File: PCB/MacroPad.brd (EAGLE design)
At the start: 76.2 x 76.2 mm, 42 parts, among them SW00 SWITCH-SMD-EVQP-P2602W, SW01 KEYSWITCH-PLAIN-MX-1U, SW02 KEYSWITCH-PLAIN-MX-1U, SW03 KEYSWITCH-PLAIN-MX-1U, SW04 KEYSWITCH-PLAIN-MX-1U, SW05 KEYSWITCH-PLAIN-MX-1U, SW06 KEYSWITCH-PLAIN-MX-1U, SW07 KEYSWITCH-PLAIN-MX-1U, SW08 KEYSWITCH-PLAIN-MX-1U, SW09 KEYSWITCH-PLAIN-MX-1U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

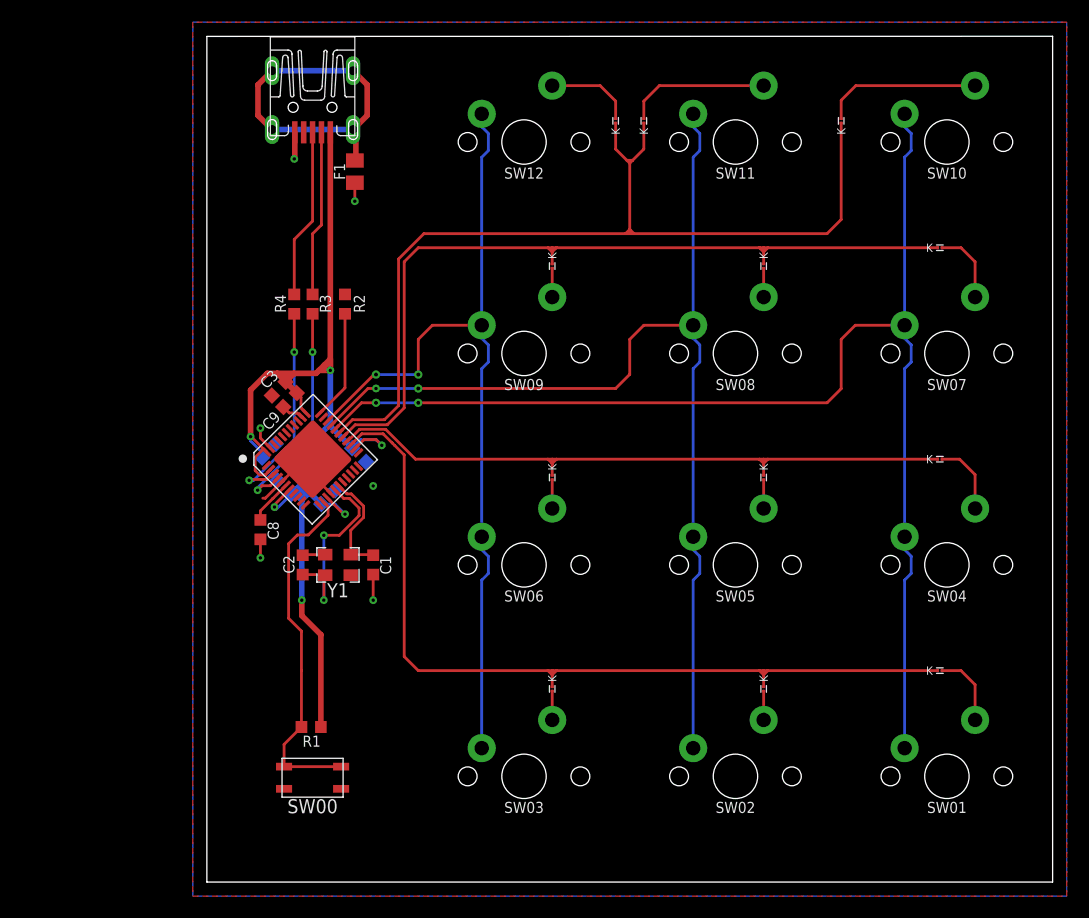
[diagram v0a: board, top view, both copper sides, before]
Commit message: Replace surface mount diodes with through hole
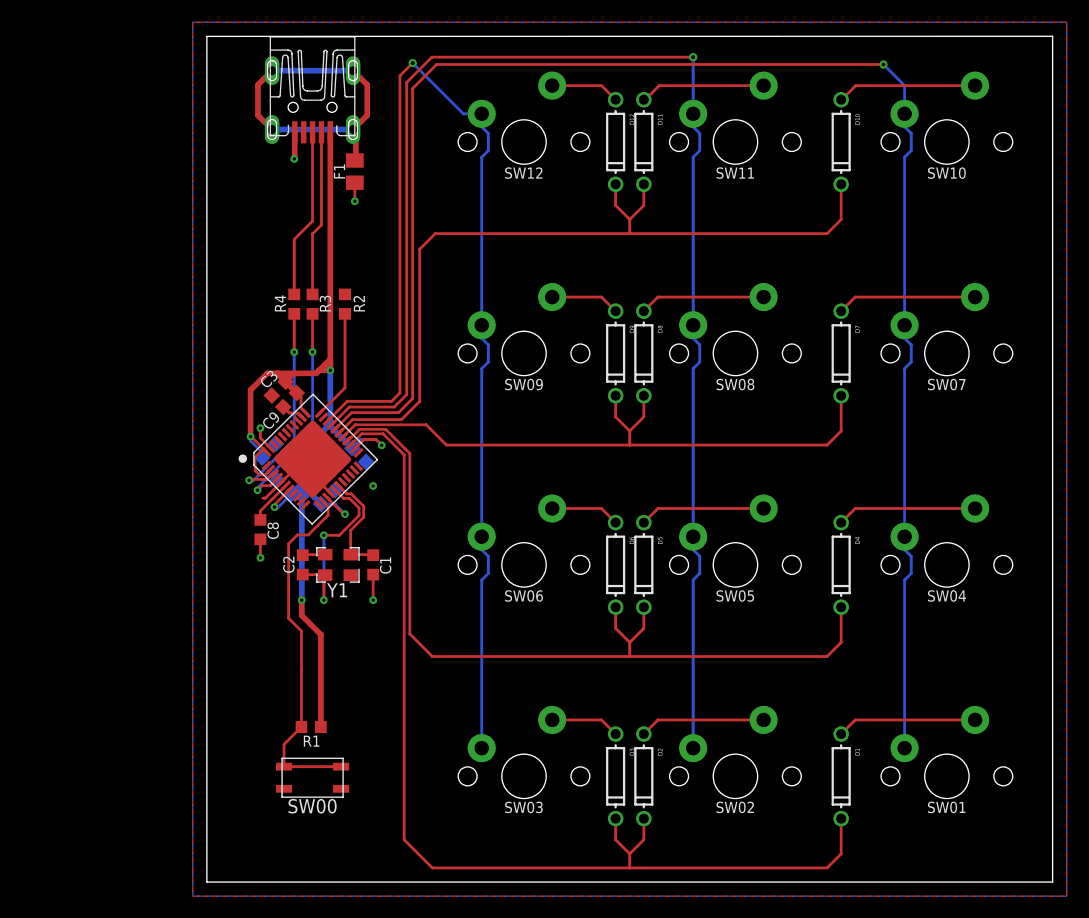
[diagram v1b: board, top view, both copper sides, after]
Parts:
- D1, D10, D11, D12, D2, D3, D4, D5, D6, D7, D8, D9: device Components:DFN0603-2 -> adafruit:DO-1N4148
- moved D8 13.4 mm to (39.4, 47.6)
- moved D2 13.4 mm to (39.4, 9.53)
- moved D5 13.4 mm to (39.4, 28.6)
- moved D1 13.0 mm to (57.1, 9.53), turned to 270 degrees
- moved D4 13.0 mm to (57.1, 28.6), turned to 270 degrees
- moved D7 13.0 mm to (57.1, 47.6), turned to 270 degrees
- moved D3 9.73 mm to (36.8, 9.53)
- moved D9 9.73 mm to (36.8, 47.6)
- moved D6 9.73 mm to (36.8, 28.6)
- moved D10 1.91 mm to (57.1, 66.7), turned to 270 degrees
- moved D11 1.91 mm to (39.4, 66.7), turned to 270 degrees
- moved D12 1.91 mm to (36.8, 66.7), turned to 270 degrees
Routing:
- net N$40: track 96.8 -> 126.6 mm, vias 2 -> 1
- net N$10: track 116.4 -> 143.2 mm, vias 2 -> 1
- net N$16: track 78.0 -> 104.5 mm, vias 2 -> 1
- net N$14: track 77.9 -> 93.5 mm
- net N$26: track 59.9 -> 75.3 mm
- net N$32: track 73.4 -> 58.5 mm
- net N$38: track 85.9 -> 73.1 mm
- net N$21: track 2.60 -> 11.3 mm
- net N$12: track 2.60 -> 11.3 mm
- net N$30: track 2.60 -> 11.3 mm
- net N$18: track 6.61 -> 12.6 mm
- net N$9: track 6.69 -> 12.6 mm
- net N$27: track 6.69 -> 12.6 mm
- net N$24: track 2.60 -> 6.24 mm
- net N$15: track 2.60 -> 6.24 mm
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
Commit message: Swap GFN for TQFP Chip -- board not updated
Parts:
- removed U$1: ATMEGA32U4-QFN44, Controller:QFN-44
- added U1: ATMEGA32U4-AUR, ATMEGA32U4-AUR:QFP80P1200X1200X120-44N
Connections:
- net GND: now also U1.15, U1.23, U1.35, U1.43, U1.5; no longer U$1.15, U$1.23, U$1.35, U$1.43, U$1.5, U$1.TAB
- net N$1: now also U1.16; no longer U$1.16
- net N$10: now also U1.29; no longer U$1.29
- net N$14: now also U1.25; no longer U$1.25
- net N$16: now also U1.31; no longer U$1.31
- net N$2: now also U1.17; no longer U$1.17
- net N$26: now also U1.26; no longer U$1.26
- net N$3: now also U1.13; no longer U$1.13
- net N$32: now also U1.27; no longer U$1.27
- net N$38: now also U1.28; no longer U$1.28
- net N$4: now also U1.33; no longer U$1.33
- net N$40: now also U1.30; no longer U$1.30
- net N$6: now also U1.3; no longer U$1.3
- net N$8: now also U1.4; no longer U$1.4
- net UCAP: now also U1.6; no longer U$1.6
- net VCC: now also U1.14, U1.2, U1.24, U1.34, U1.44, U1.7; no longer U$1.14, U$1.2, U$1.24, U$1.34, U$1.44, U$1.7
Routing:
- net N$3: track 32.4 -> 7.14 mm
- net VCC: track 112.6 -> 100.3 mm
- net GND: track 24.0 -> 13.7 mm, vias 6 -> 5
- net N$4: track 9.91 -> 0.00 mm
- net N$16: track 104.5 -> 102.0 mm
- net N$40: track 126.6 -> 124.2 mm
- net N$10: track 143.2 -> 141.1 mm
- net N$38: track 73.1 -> 71.4 mm
- net UCAP: track 4.09 -> 2.42 mm
- net N$32: track 58.5 -> 56.9 mm
- net N$14: track 93.5 -> 92.1 mm
- net N$1: track 17.7 -> 16.5 mm
- net N$2: track 9.90 -> 8.85 mm

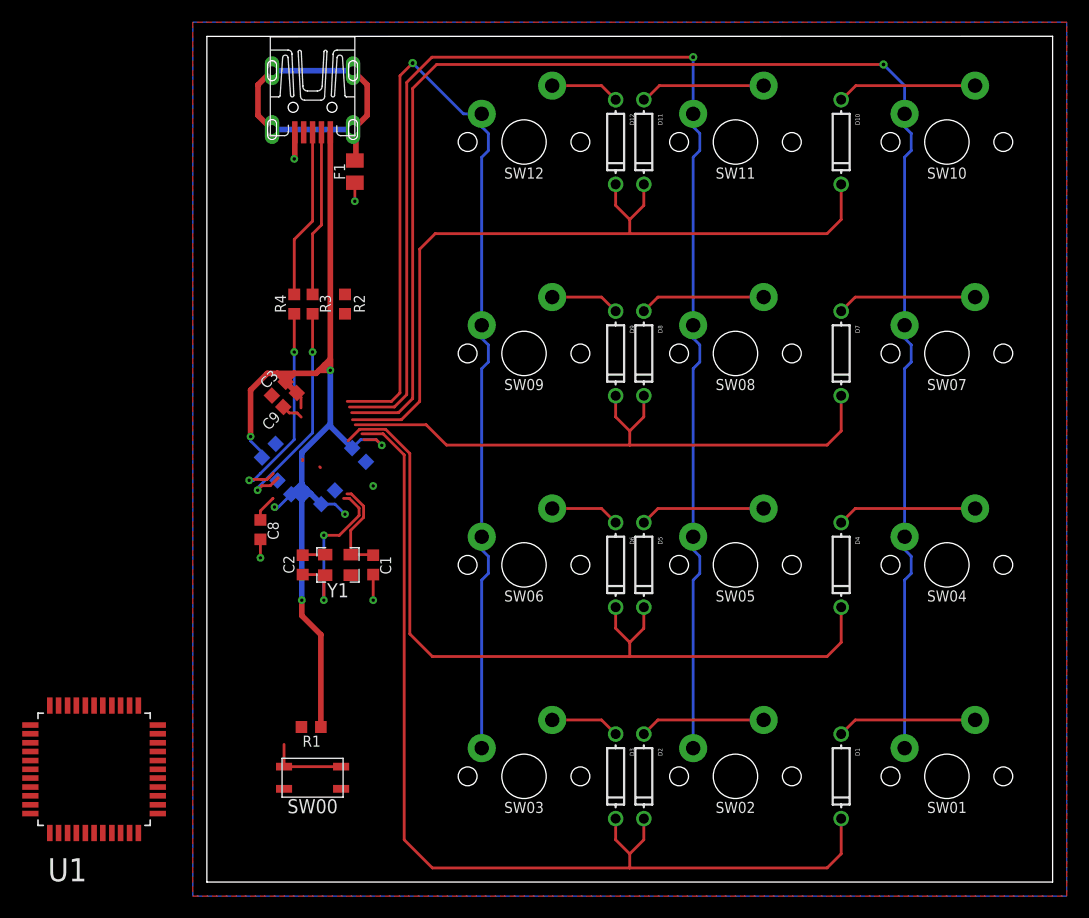
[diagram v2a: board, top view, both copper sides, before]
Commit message: Update board for TQFP footprint
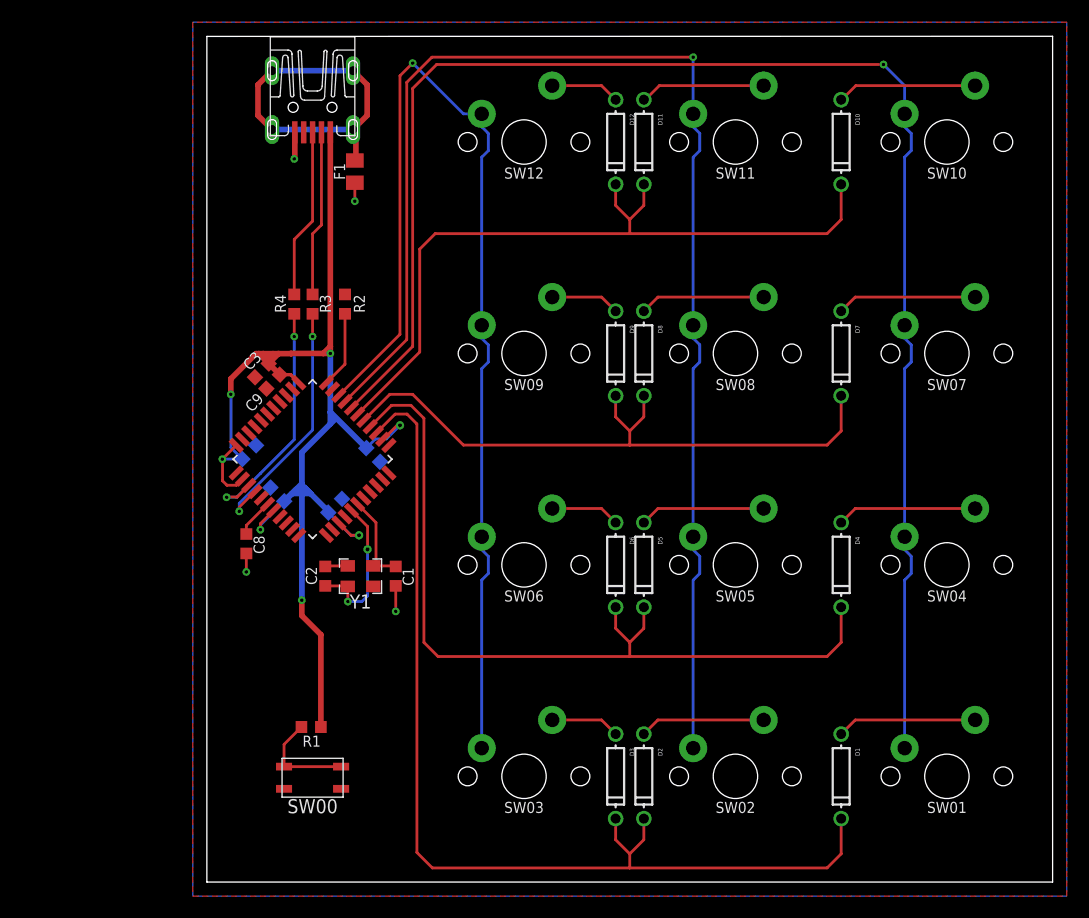
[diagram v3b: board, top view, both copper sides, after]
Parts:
- moved U1 34.2 mm to (9.53, 38.1), turned to 45 degrees
- moved C1 2.27 mm to (17.0, 27.6)
- moved C2 2.27 mm to (10.7, 27.6)
- moved Y1 2.27 mm to (13.8, 27.6)
- moved C9 2.25 mm to (5.97, 45.1)
- moved C3 2.25 mm to (4.95, 46.1)
- moved C8 1.80 mm to (3.56, 30.5)
- moved C5 1.78 mm to (3.81, 38.7)
- moved C7 1.27 mm to (15.0, 38.5)
- moved C6 0.99 mm to (11.6, 33.9)
- moved C4 0.90 mm to (6.35, 34.9)
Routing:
- net VCC: track 100.3 -> 124.5 mm, vias 6 -> 7
- net N$4: track 0.00 -> 6.91 mm
- net N$38: track 71.4 -> 68.1 mm
- net N$10: track 141.1 -> 138.2 mm
- net N$1: track 16.5 -> 13.7 mm
- net N$40: track 124.2 -> 121.5 mm
- net N$8: track 20.3 -> 22.9 mm
- net N$16: track 102.0 -> 99.4 mm
- net N$6: track 19.5 -> 22.0 mm
- net N$14: track 92.1 -> 94.5 mm
- net GND: track 13.7 -> 11.4 mm, vias 5 -> 4
- net N$3: track 7.14 -> 9.36 mm
- net N$26: track 75.2 -> 76.8 mm
- net N$32: track 56.9 -> 58.2 mm
- net UCAP: track 2.42 -> 3.48 mm
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
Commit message: Use 5x3.2mm crystal
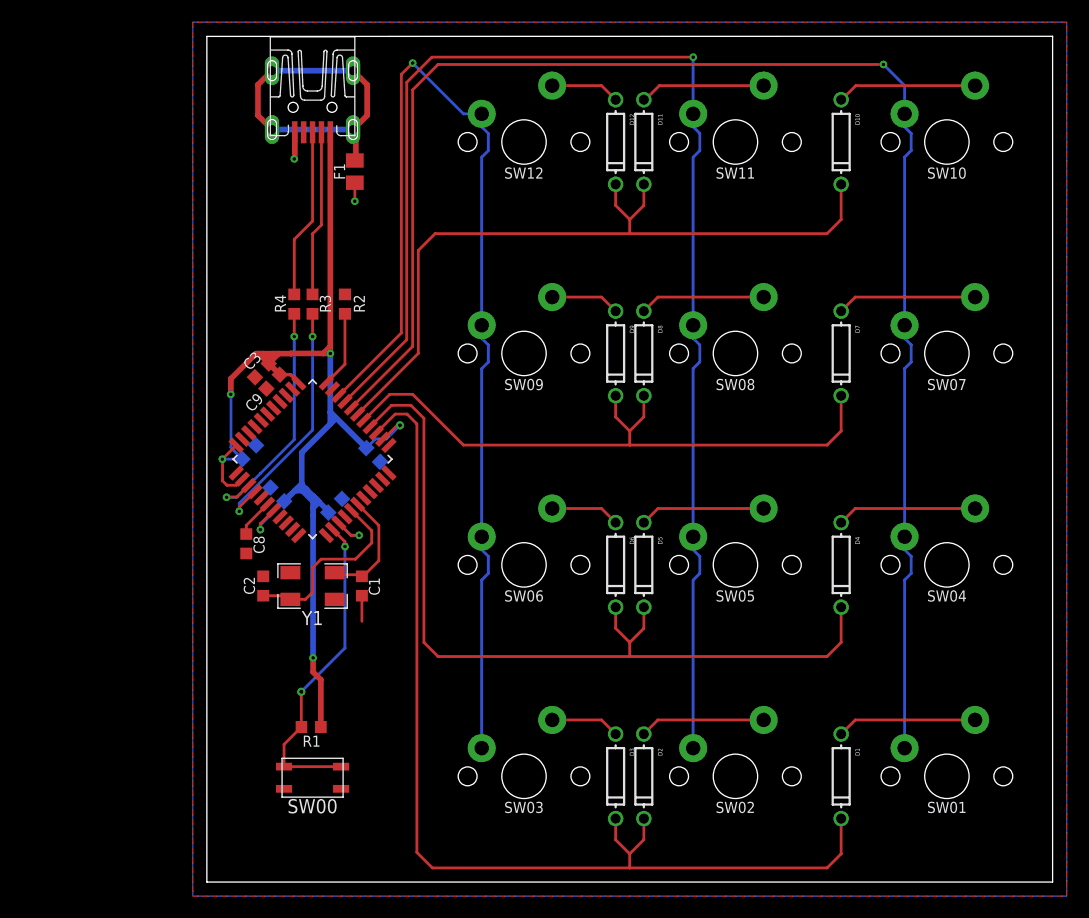
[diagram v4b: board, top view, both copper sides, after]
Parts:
- Y1: device Components:CRYSTAL-3.2X2.5 -> Controller:CRYSTAL-3.2X5
- moved C2 5.66 mm to (5.08, 26.7)
- moved Y1 4.41 mm to (9.53, 26.7)
- moved C1 3.18 mm to (14.0, 26.7)
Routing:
- net N$3: track 9.36 -> 29.3 mm, vias 0 -> 2
- net GND: track 11.4 -> 7.25 mm, vias 4 -> 2
- net N$1: track 13.7 -> 17.0 mm, vias 2 -> 0
- net N$2: track 8.29 -> 10.8 mm
- net VCC: track 124.5 -> 122.4 mm
